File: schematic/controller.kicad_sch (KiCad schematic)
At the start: 8 parts, among them J5 Player 1, J7 Player 2

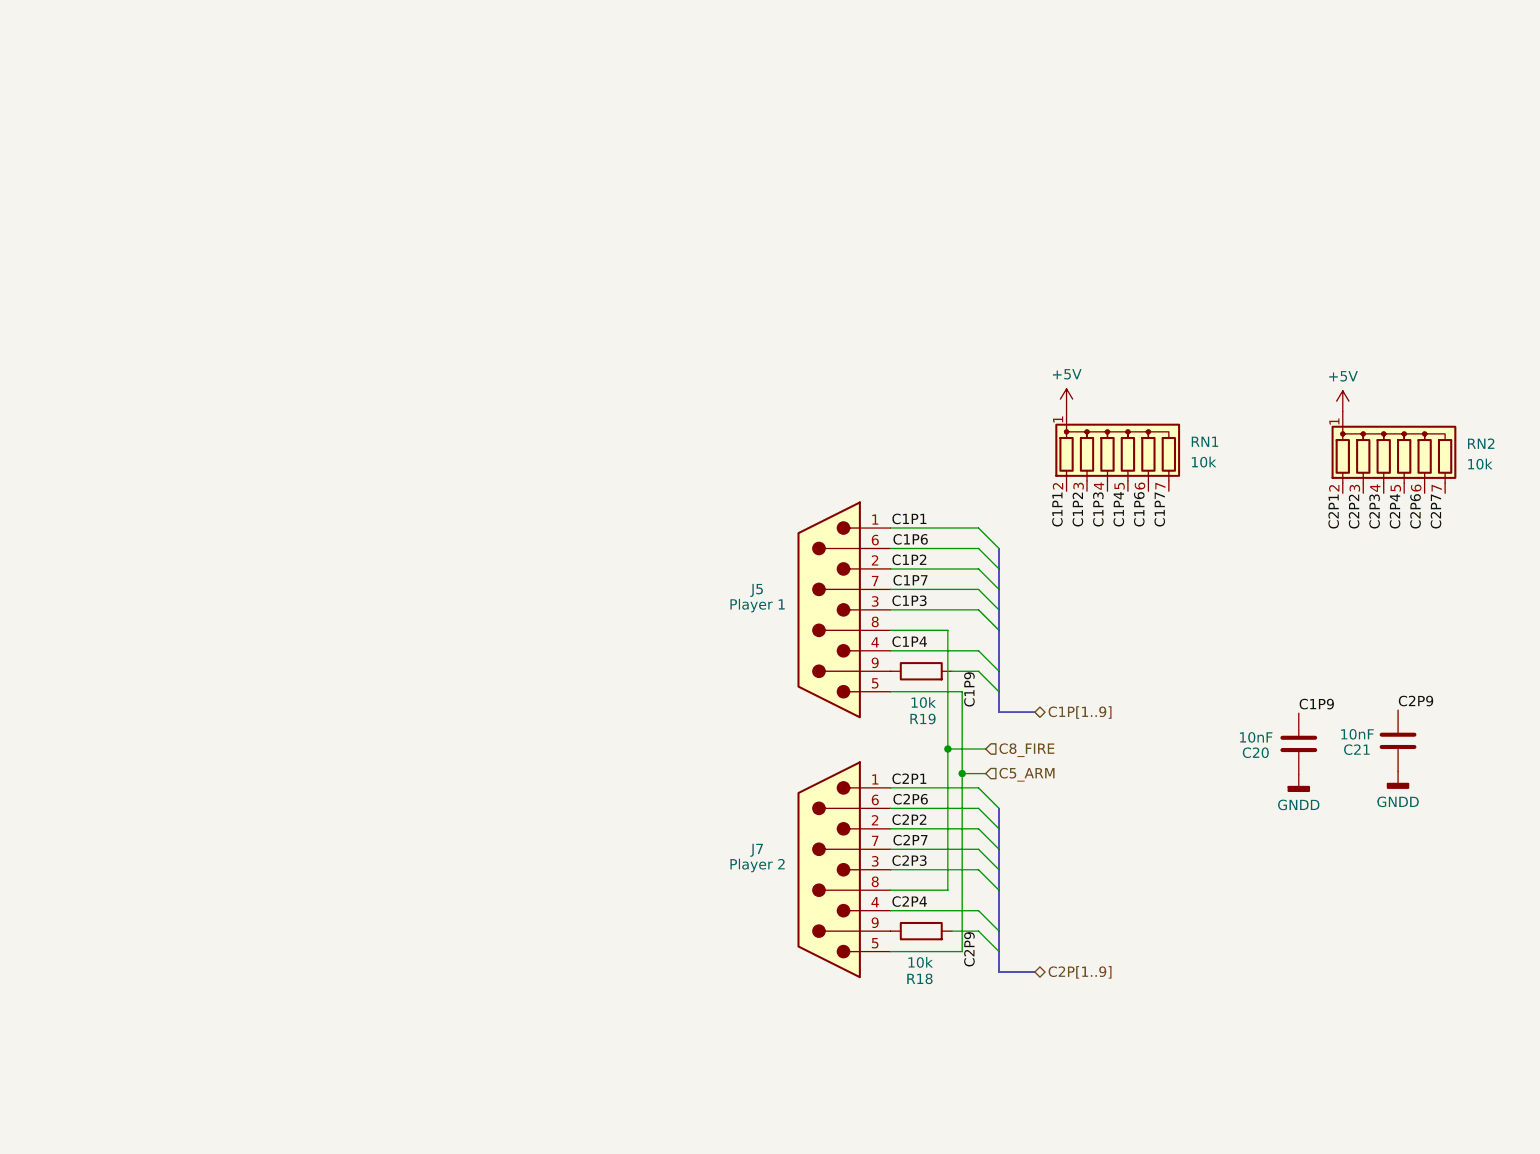
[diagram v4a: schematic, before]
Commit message: first commit with PCB revised for super game module. Needs model updates and tweaks
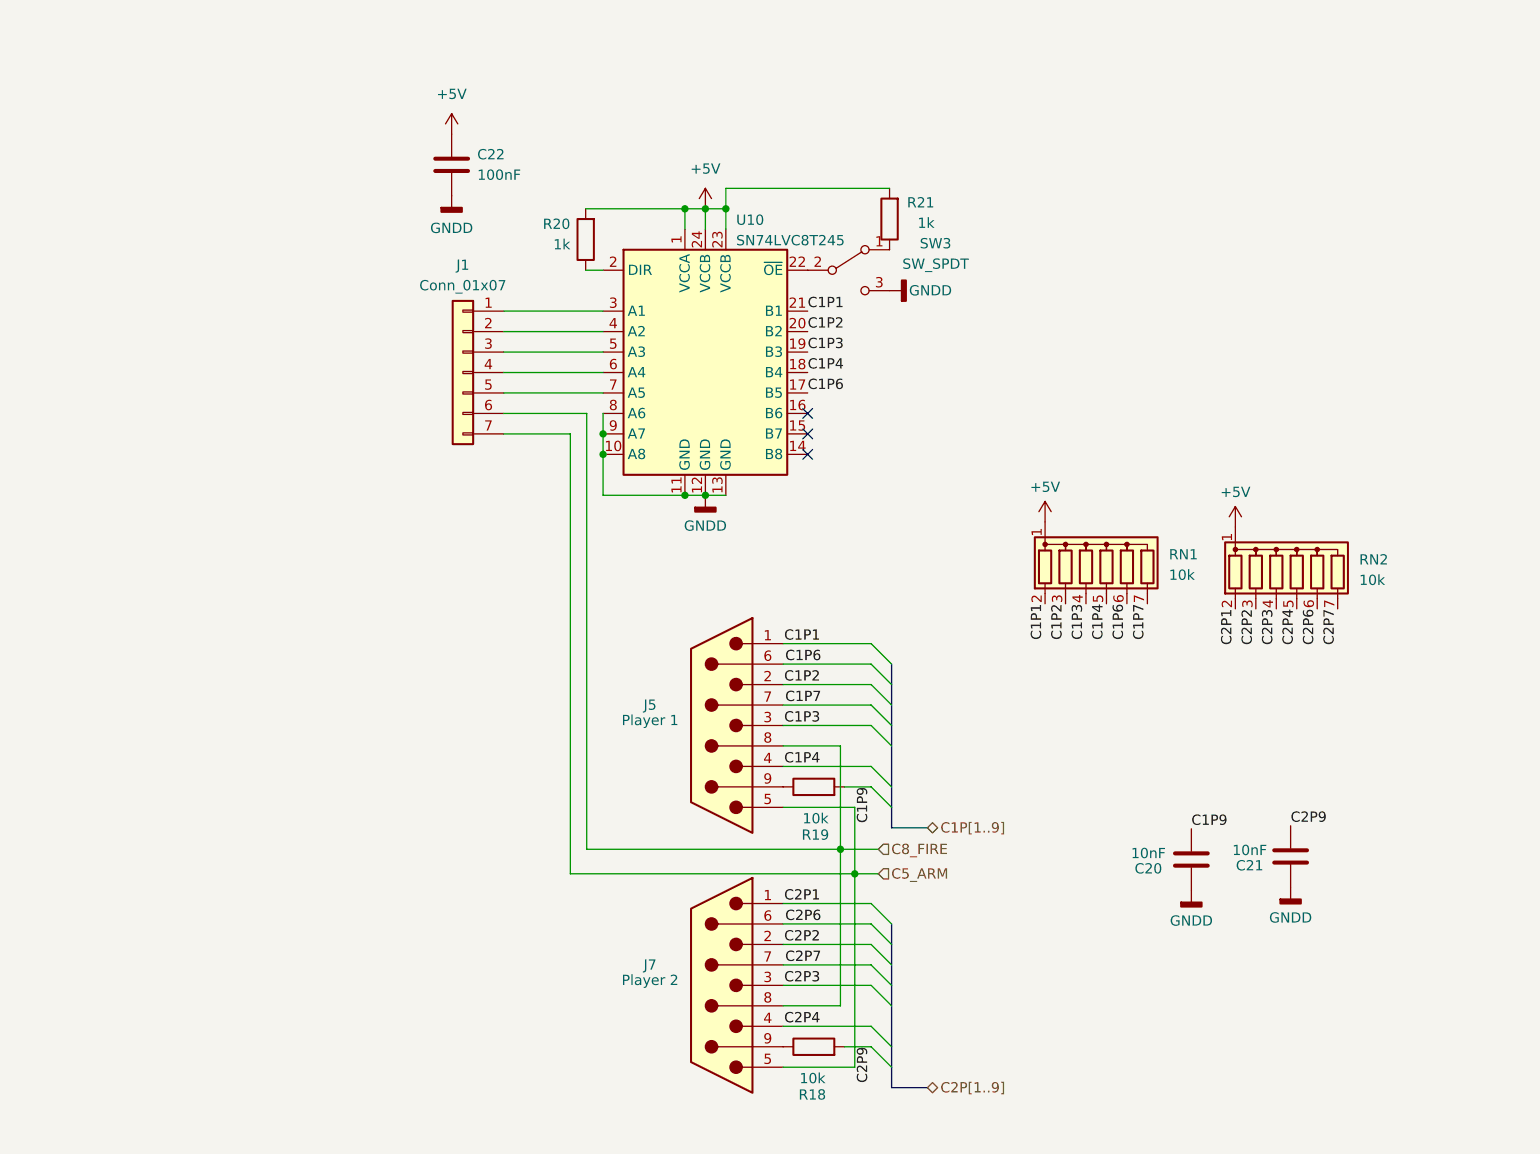
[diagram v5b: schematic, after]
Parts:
- added C22: 100nF, Capacitor_SMD:C_1206_3216Metric, symbol Device:C
- added J1: Conn_01x07, Connector_PinHeader_2.54mm:PinHeader_1x07_P2.54mm_Vertical, symbol Connector_Generic:Conn_01x07
- added R20, R21: 1k, Resistor_SMD:R_0805_2012Metric, symbol Device:R
- added SW3: SW_SPDT, Switches_THT:SW_CuK_OS102011MA1QN1_SPDT_Angled, symbol Switch:SW_SPDT
- added U10: SN74LVC8T245, Package_SO:TSSOP-24_4.4x7.8mm_P0.65mm, symbol Logic_Level_Translator:SN74LVC8T245
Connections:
- net +5V: now also C22.1, R20.2, R21.2, U10.1 (VCCA), U10.23 (VCCB), U10.24 (VCCB)
- net C1P1: now also U10.21 (B1)
- net C1P2: now also U10.20 (B2)
- net C1P3: now also U10.19 (B3)
- net C1P4: now also U10.18 (B4)
- net C1P6: now also U10.17 (B5)
- net C5_ARM: now also J1.7 (Pin_7)
- net C8_FIRE: now also J1.6 (Pin_6)
- net GNDD: now also C22.2, SW3.3 (C), U10.10 (A8), U10.11 (GND), U10.12 (GND), U10.13 (GND), U10.8 (A6), U10.9 (A7)
- new net: R21.1, SW3.1 (A)
- new net: SW3.2 (B), U10.22 (~{OE})
- new net: J1.1 (Pin_1), U10.3 (A1)
- new net: J1.2 (Pin_2), U10.4 (A2)
- new net: J1.3 (Pin_3), U10.5 (A3)
- new net: J1.4 (Pin_4), U10.6 (A4)
- new net: J1.5 (Pin_5), U10.7 (A5)
- new net: R20.1, U10.2 (DIR)
- no-connect marks 0 -> 3
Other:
- moved on the sheet: C20, C21, J5, J7, R18, R19, RN1, RN2

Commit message: tweaks to routing to help make better grounds
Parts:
- R21: footprint Resistor_SMD:R_0805_2012Metric -> Resistor_THT:R_Axial_DIN0207_L6.3mm_D2.5mm_P10.16mm_Horizontal
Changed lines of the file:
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@@
       (effects (font (size 1.27 1.27)) (justify left))
     )
-    (property "Footprint" "Resistor_SMD:R_0805_2012Metric" (at 143.51 43.815 90)
+    (property "Footprint" "Resistor_THT:R_Axial_DIN0207_L6.3mm_D2.5mm_P10.16mm_Horizontal" (at 143.51 43.815 90)
       (effects (font (size 1.27 1.27)) hide)
     )

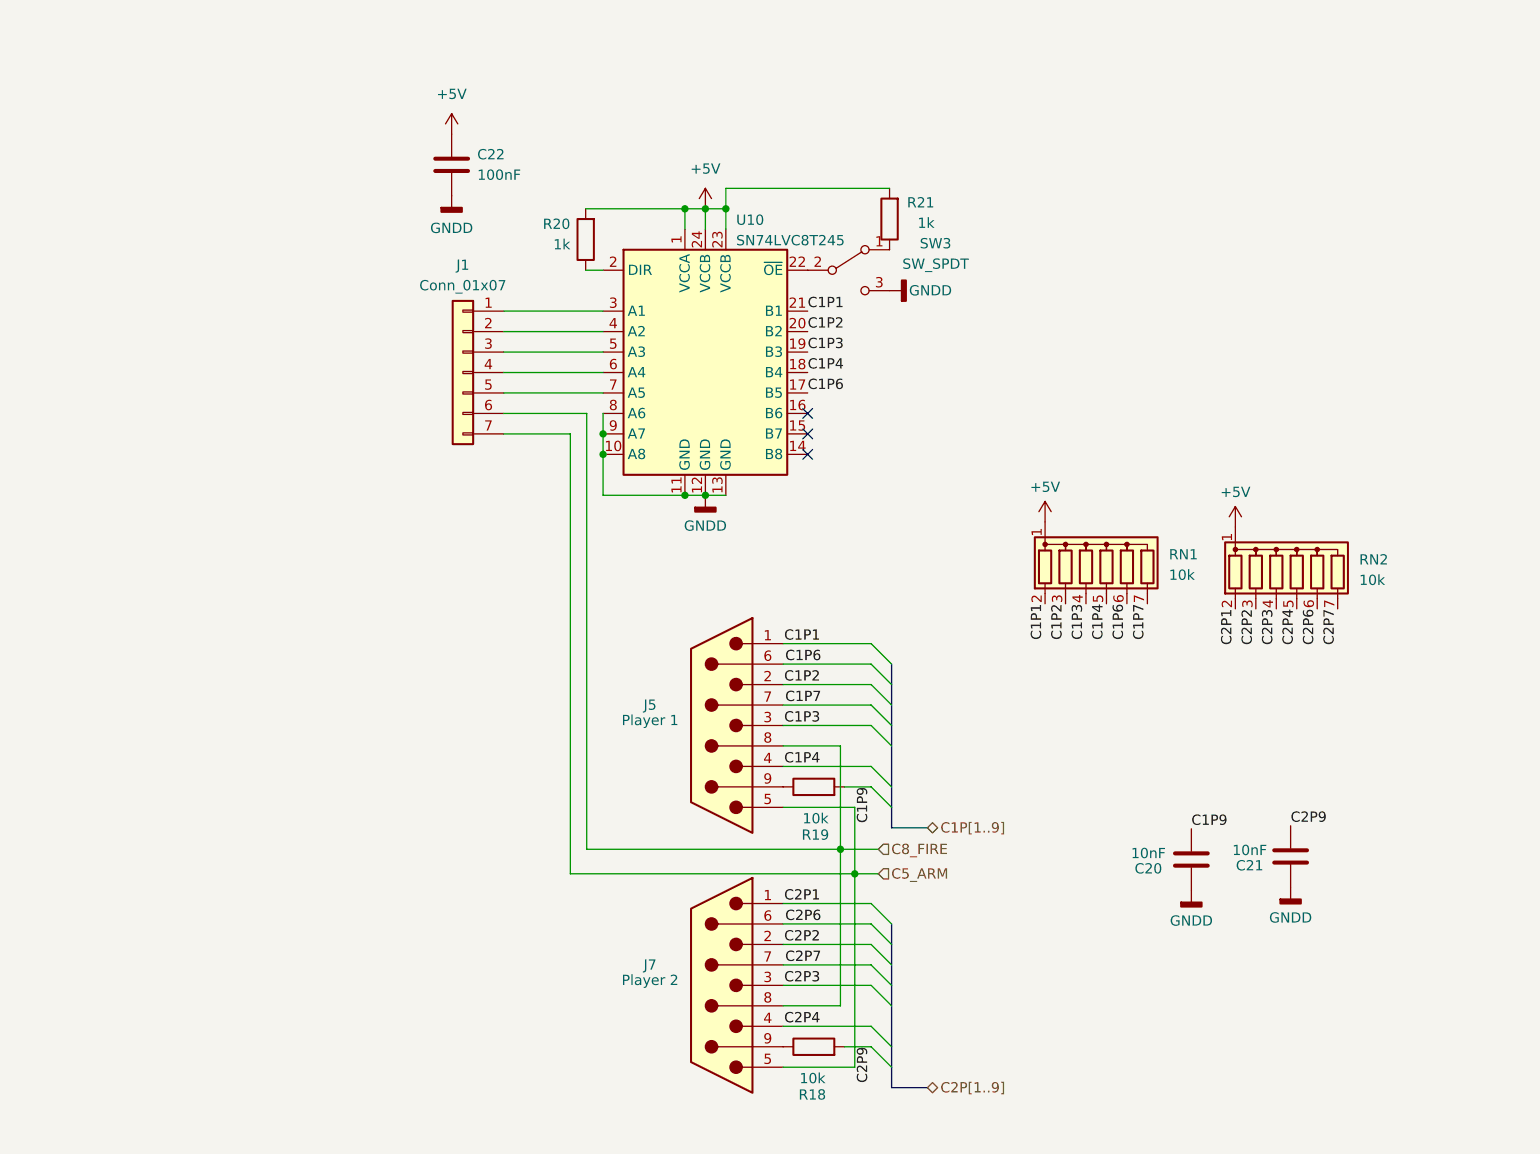
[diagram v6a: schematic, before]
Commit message: revised controller select circuit
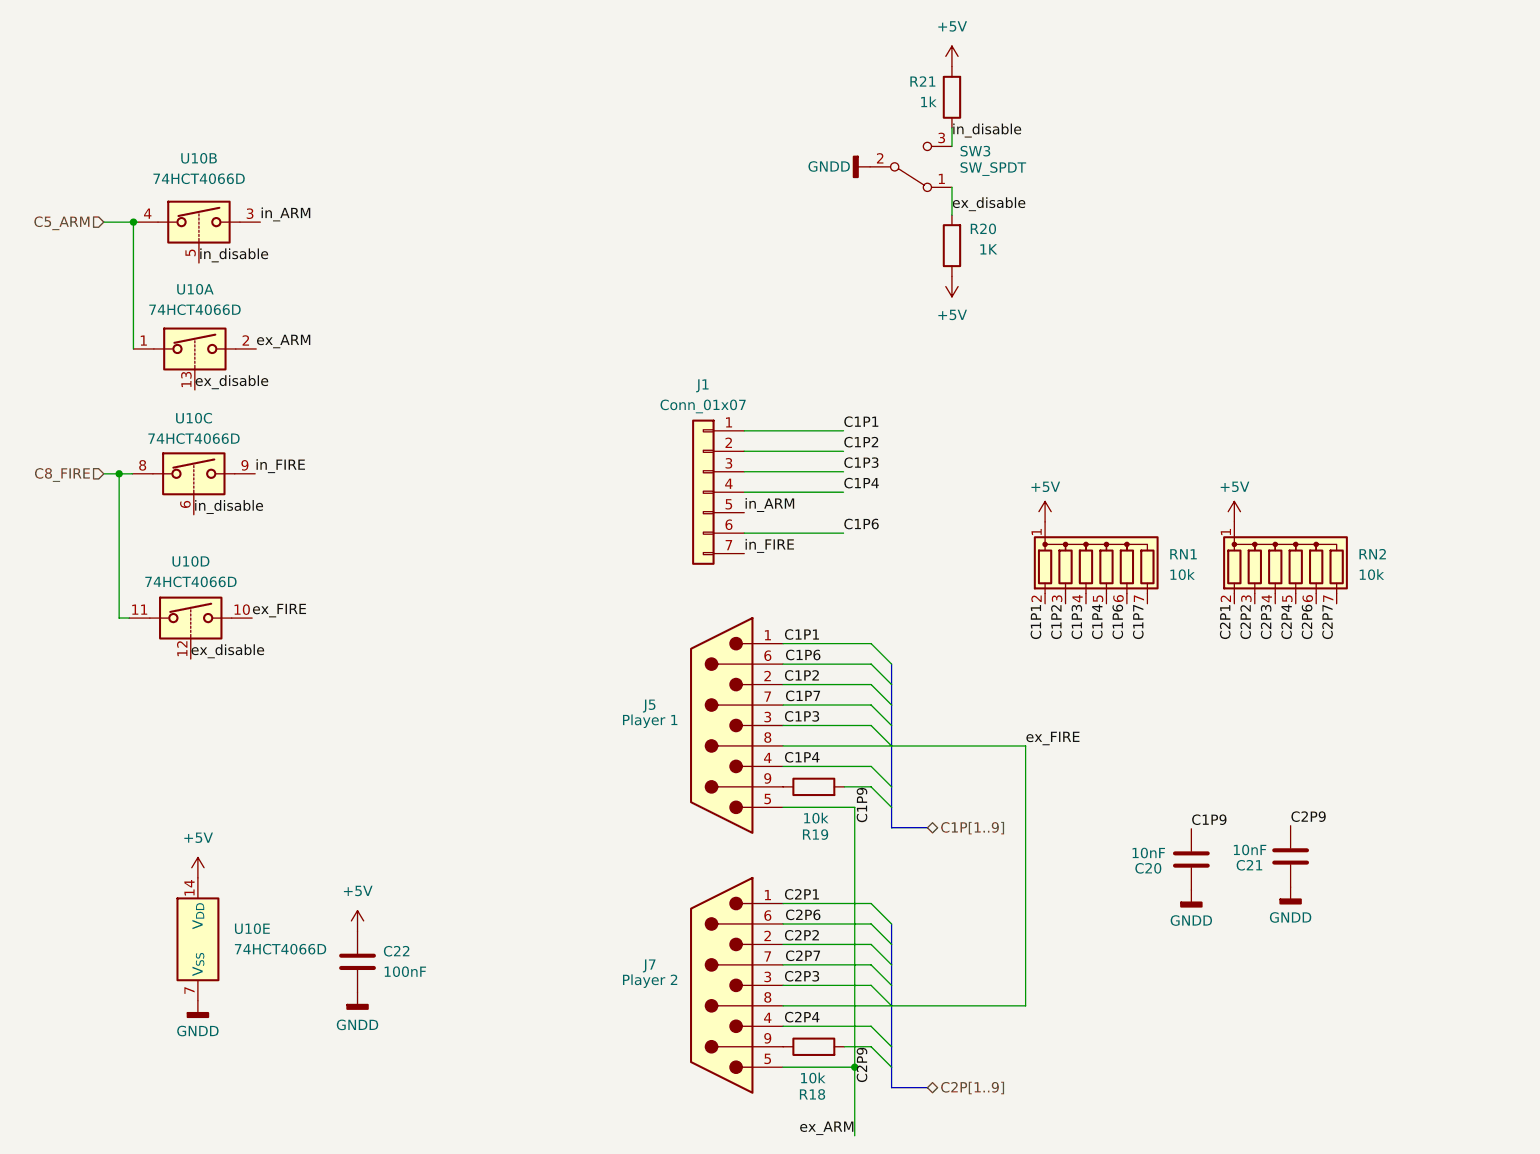
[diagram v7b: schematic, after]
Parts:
- removed U10: SN74LVC8T245, Package_SO:TSSOP-24_4.4x7.8mm_P0.65mm, symbol Logic_Level_Translator:SN74LVC8T245
- added U10: 74HCT4066D, Package_SO:SO-14_3.9x8.65mm_P1.27mm, symbol Analog_Switch:CD4066BM
- R20: renamed from R21; value 1k -> 1K; footprint Resistor_THT:R_Axial_DIN0207_L6.3mm_D2.5mm_P10.16mm_Horizontal -> Resistor_SMD:R_0805_2012Metric
- renumbered R20 to R21
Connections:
- net +5V: now also R20.1, U10.14 (V_{DD}); no longer R20.2
- net C1P1: now also J1.1 (Pin_1)
- net C1P2: now also J1.2 (Pin_2)
- net C1P3: now also J1.3 (Pin_3)
- net C1P4: now also J1.4 (Pin_4)
- net C1P6: now also J1.6 (Pin_6)
- net C5_ARM: now also U10.1, U10.4; no longer J1.7 (Pin_7), J5.5, J7.5
- net C8_FIRE: now also U10.11, U10.8; no longer J1.6 (Pin_6), J5.8, J7.8
- net GNDD: now also SW3.2 (B), U10.7 (V_{SS}); no longer SW3.3 (C)
- net ex_disable: now reaches SW3.1 (A)
- net ex_disable: now also R20.2, U10.12, U10.13; no longer R20.1
- net in_ARM: now reaches J1.5 (Pin_5)
- net in_ARM: now also U10.3
- net in_disable: now reaches R21.1
- net in_disable: now also SW3.3 (C), U10.5, U10.6
- new net ex_ARM: J5.5, J7.5, U10.2
- new net ex_FIRE: J5.8, J7.8, U10.10
- new net in_FIRE: J1.7 (Pin_7), U10.9
- no-connect marks 3 -> 0
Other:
- moved on the sheet: C22, J1, R20, R21, RN2, SW3

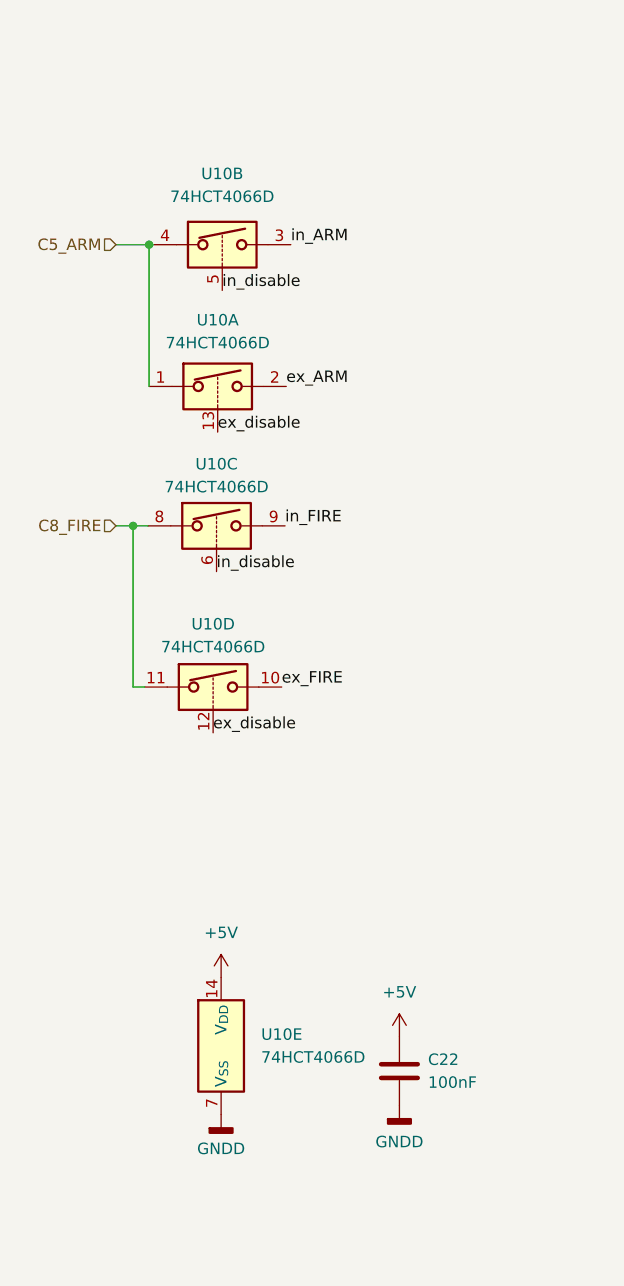
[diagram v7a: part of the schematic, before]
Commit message: changed IC to 74ABT125 for higher current, and just makes sense to use a TTL buffer instead of a analog switch
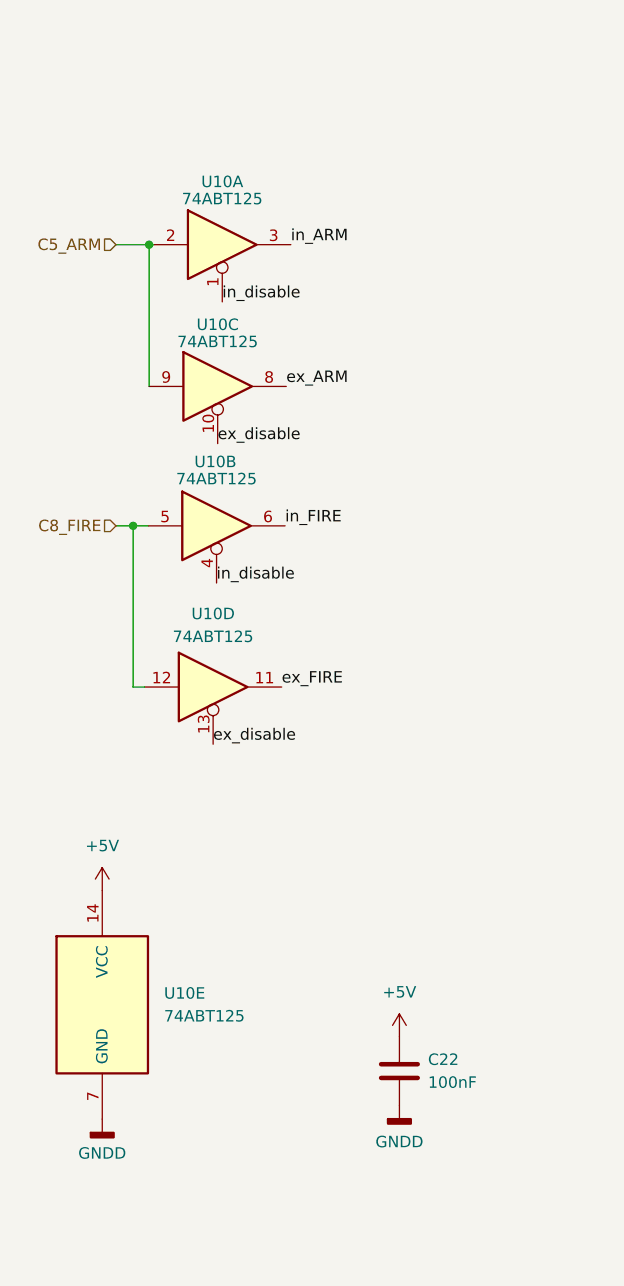
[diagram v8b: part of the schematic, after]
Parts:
- removed U10: 74HCT4066D, Package_SO:SO-14_3.9x8.65mm_P1.27mm, symbol Analog_Switch:CD4066BM
- added U10: 74ABT125, Package_SO:SOIC-14_3.9x8.7mm_P1.27mm, symbol 74xx:74LS125
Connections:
- net +5V: now also U10.14 (VCC)
- net C5_ARM: now also U10.2, U10.9
- net C8_FIRE: now also U10.12, U10.5
- net GNDD: now also U10.7 (GND)
- net ex_ARM: now also U10.8
- net ex_FIRE: now also U10.11
- net ex_disable: now also U10.10, U10.13
- net in_ARM: now also U10.3
- net in_FIRE: now also U10.6
- net in_disable: now also U10.1, U10.4
